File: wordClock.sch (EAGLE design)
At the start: 30 parts, among them J1 SPI_PRG, Q1 MOSFET-PCHANNELSMD, Q2 MOSFET-PCHANNELSMD, Q3 MOSFET-PCHANNELSMD, Q4 MOSFET-PCHANNELSMD, Q5 MOSFET-PCHANNELSMD, Q6 MOSFET-PCHANNELSMD, Q7 MOSFET-PCHANNELSMD, Q8 MOSFET-PCHANNELSMD, U1 ATMEGA328P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

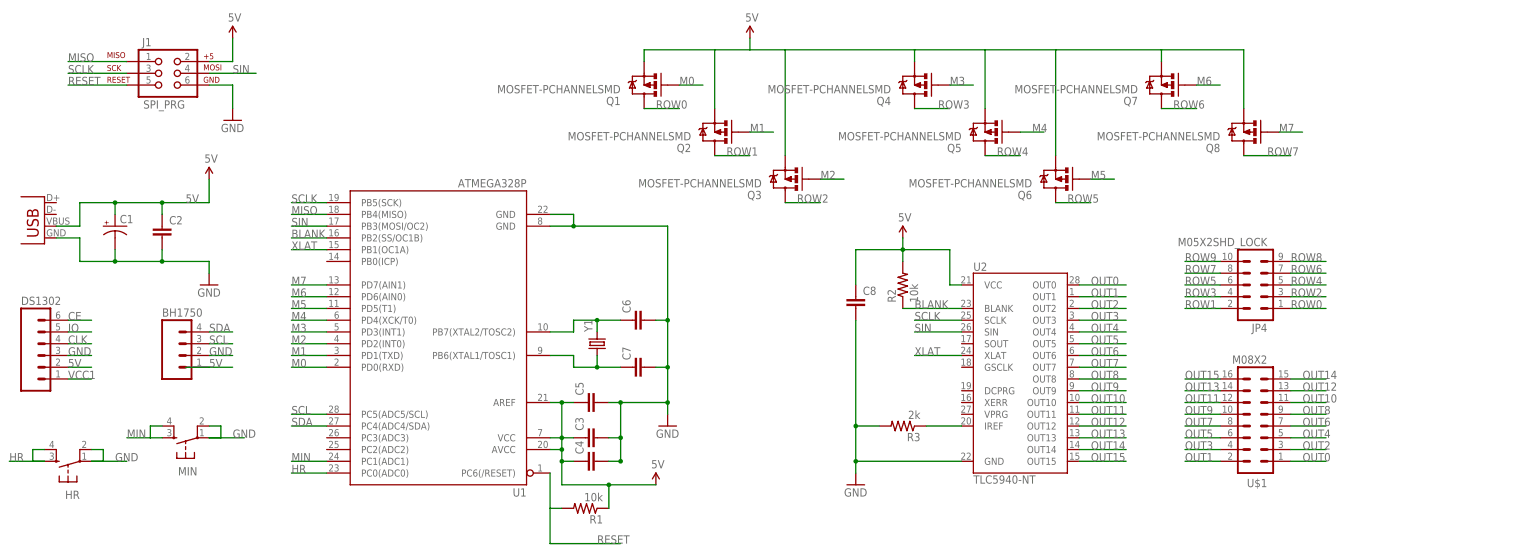
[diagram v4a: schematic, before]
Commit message: Added pullup resistors to all P-mosfets
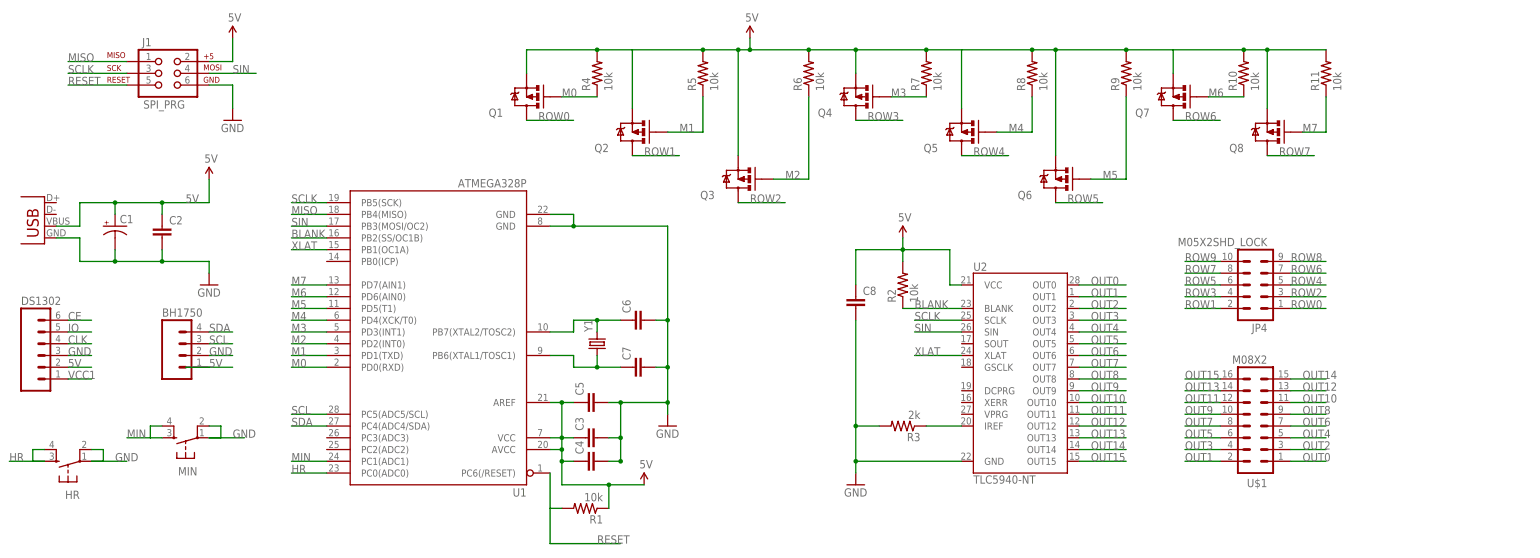
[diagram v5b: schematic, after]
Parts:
- added R10, R11, R4, R5, R6, R7, R8, R9: 10k, SparkFun-Passives:RESISTOR0805-RES
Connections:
- net 5V: now also R10.2, R11.2, R4.2, R5.2, R6.2, R7.2, R8.2, R9.2
- net M0: now also R4.1
- net M1: now also R5.1
- net M2: now also R6.1
- net M3: now also R7.1
- net M4: now also R8.1
- net M5: now also R9.1
- net M6: now also R10.1
- net M7: now also R11.1
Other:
- moved on the sheet: Q1, Q2, Q3, Q4, Q5, Q7, Q8
